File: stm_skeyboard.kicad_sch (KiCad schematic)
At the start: 0 parts

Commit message: adjust paths for kicanvas
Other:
- sheet main: file sheets/mcu.kicad_sch -> mcu.kicad_sch
- sheet matrix: file sheets/matrix.kicad_sch -> matrix.kicad_sch
- company: (none) -> https://github.com/Challmymind
- title: (none) -> Keyboard based on STM32L0xx
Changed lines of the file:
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@@
 	(generator_version "8.0")
 	(paper "A4")
+	(title_block
+		(title "Keyboard based on STM32L0xx")
+		(date "2024-04-28")
+		(rev "0.1")
+		(company "https://github.com/Challmymind")
+	)
 	(wire
 		(pts
@@
 			)
 		)
-		(property "Sheetfile" "sheets/matrix.kicad_sch"
+		(property "Sheetfile" "matrix.kicad_sch"
 			(at 184.15 104.7246 0)
 			(effects
@@
 			)
 		)
-		(property "Sheetfile" "sheets/mcu.kicad_sch"
+		(property "Sheetfile" "mcu.kicad_sch"
 			(at 91.44 80.5946 0)
 			(effects

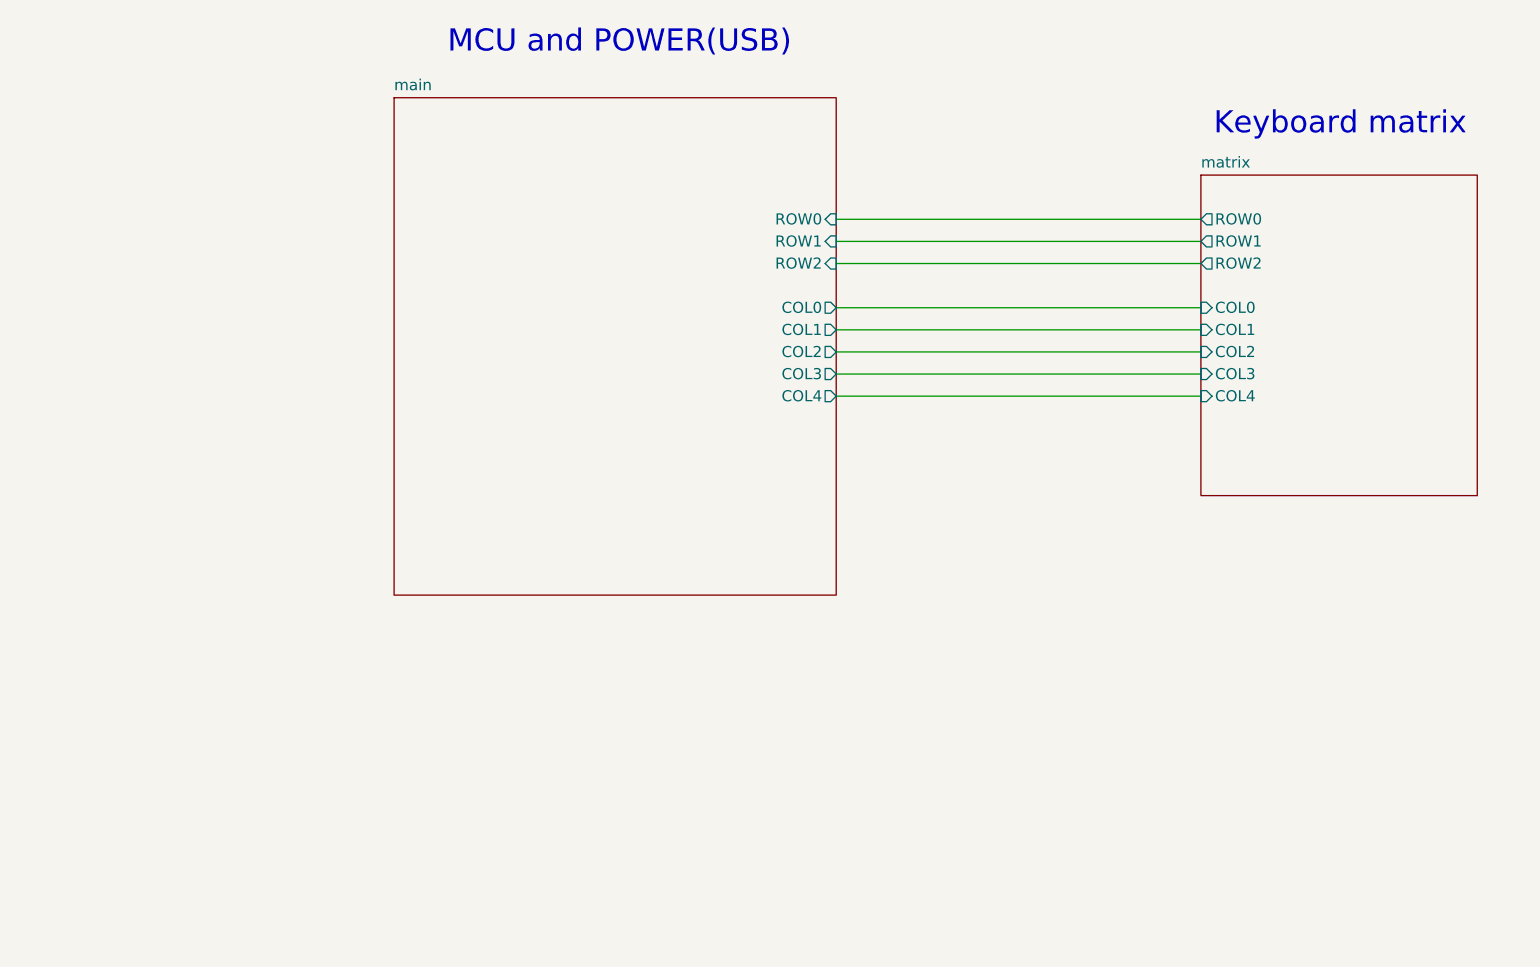
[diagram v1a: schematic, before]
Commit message: moved usb to another sheet, cleared ERC violations
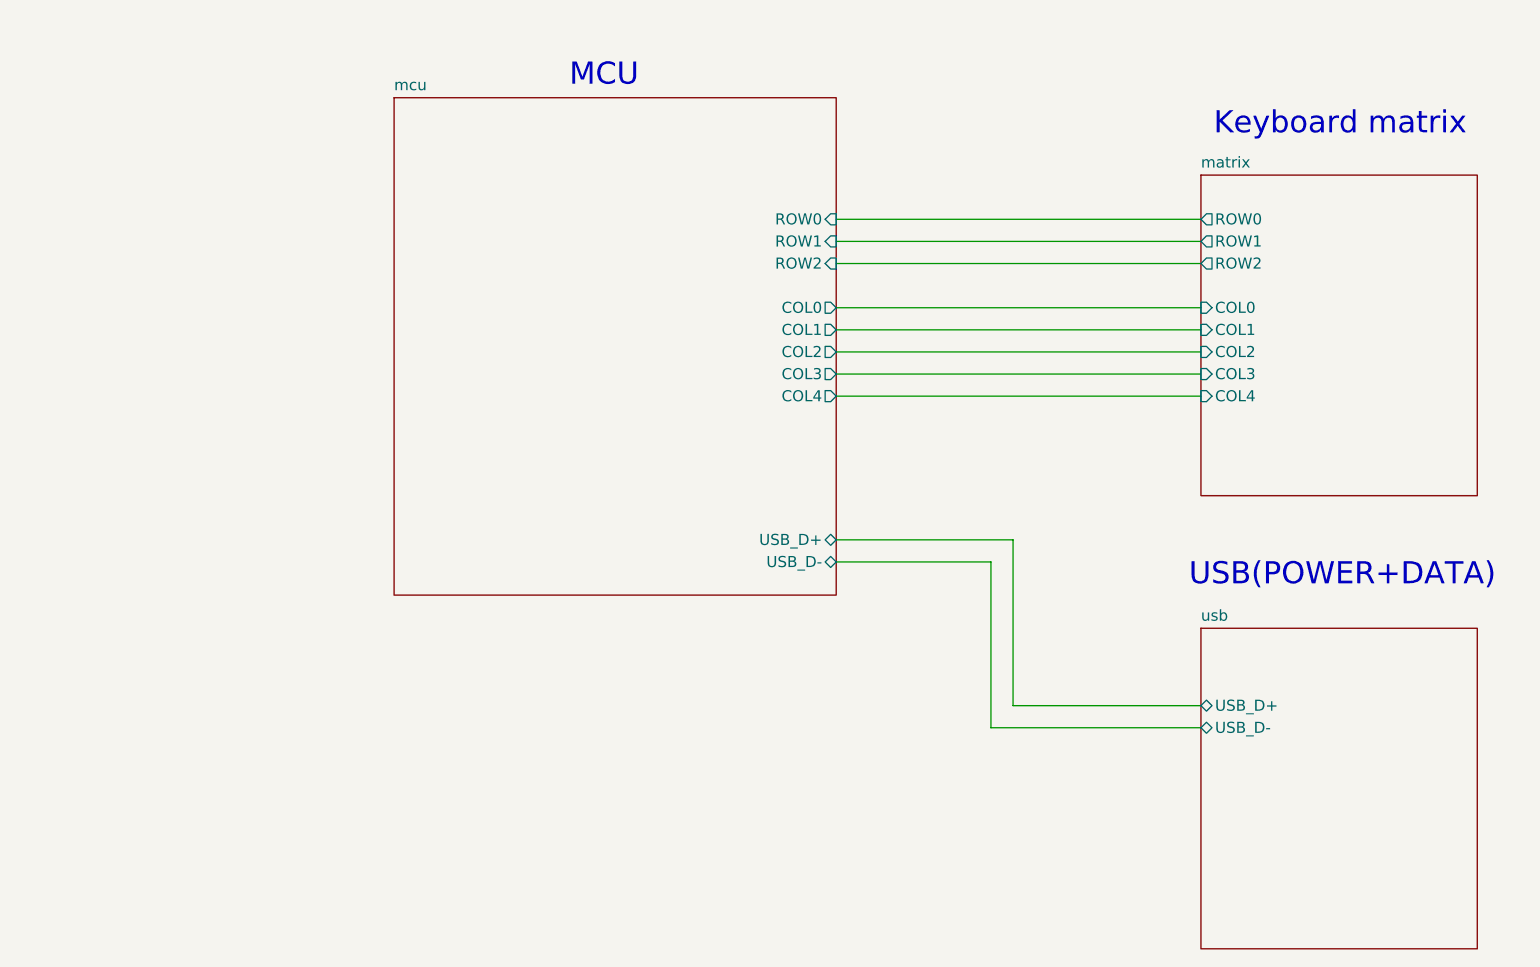
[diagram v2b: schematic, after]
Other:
- sheet main renamed mcu
- added sheet usb (usb.kicad_sch)
- sheet mcu ports: added USB_D+, USB_D-; removed none
- note added: "MCU"
- note added: "USB(POWER+DATA)"
- note removed: "MCU and POWER(USB)"
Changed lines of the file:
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@@
+	(wire
+		(pts
+			(xy 160.02 111.76) (xy 160.02 130.81)
+		)
+		(stroke
+			(width 0)
+			(type default)
+		)
+	)
 	(wire
 		(pts
@@
 	(wire
 		(pts
+			(xy 162.56 109.22) (xy 162.56 128.27)
+		)
+		(stroke
+			(width 0)
+			(type default)
+		)
+	)
+	(wire
+		(pts
+			(xy 142.24 109.22) (xy 162.56 109.22)
+		)
+		(stroke
+			(width 0)
+			(type default)
+		)
+	)
+	(wire
+		(pts
+			(xy 160.02 130.81) (xy 184.15 130.81)
+		)
+		(stroke
+			(width 0)
+			(type default)
+		)
+	)
+	(wire
+		(pts
 			(xy 142.24 87.63) (xy 184.15 87.63)
 		)
@@
 	(wire
 		(pts
+			(xy 142.24 111.76) (xy 160.02 111.76)
+		)
+		(stroke
+			(width 0)
+			(type default)
+		)
+	)
+	(wire
+		(pts
 			(xy 142.24 90.17) (xy 184.15 90.17)
 		)
@@
 	(wire
 		(pts
+			(xy 162.56 128.27) (xy 184.15 128.27)
+		)
+		(stroke
+			(width 0)
+			(type default)
+		)
+	)
+	(wire
+		(pts
 			(xy 142.24 82.55) (xy 184.15 82.55)
 		)
@@
 		)
 	)
-	(text "MCU and POWER(USB)\n"
+	(text "MCU"
 		(exclude_from_sim no)
-		(at 117.348 52.07 0)
+		(at 115.57 55.88 0)
 		(effects
 			(font
@@
 		)
 	)
+	(text "USB(POWER+DATA)"
+		(exclude_from_sim no)
+		(at 200.406 113.284 0)
+		(effects
+			(font
+				(size 2.54 2.54)
+			)
+		)
+	)
 	(sheet
 		(at 184.15 67.31)
@@
 	)
 	(sheet
+		(at 184.15 119.38)
+		(size 31.75 36.83)
+		(fields_autoplaced yes)
+		(stroke
+			(width 0.1524)
+			(type solid)
+		)
+		(fill
+			(color 255 255 194 1.0000)
+		)
+		(property "Sheetname" "usb"
+			(at 184.15 118.6684 0)
+			(effects
+				(font
+					(size 1.27 1.27)
+				)
+				(justify left bottom)
+			)
+		)
+		(property "Sheetfile" "usb.kicad_sch"
+			(at 184.15 156.7946 0)
+			(effects
+				(font
+					(size 1.27 1.27)
+				)
+				(justify left top)
+				(hide yes)
+			)
+		)
+		(pin "USB_D+" bidirectional
+			(at 184.15 128.27 180)
+			(effects
+				(font
+					(size 1.27 1.27)
+				)
+				(justify left)
+			)
+		)
+		(pin "USB_D-" bidirectional
+			(at 184.15 130.81 180)
+			(effects
+				(font
+					(size 1.27 1.27)
+				)
+				(justify left)
+			)
+		)
+		(instances
+			(project "stm_skeyboard"
+				(path "/f8cbad95-1fac-4ee0-b4c1-fc27b4678331"
+					(page "4")
+				)
+			)
+		)
+	)
+	(sheet
 		(at 91.44 58.42)
 		(size 50.8 57.15)
@@
 			(color 255 255 194 1.0000)
 		)
-		(property "Sheetname" "main"
+		(property "Sheetname" "mcu"
 			(at 91.44 57.7084 0)
 			(effects
@@
 			(effects
 				(font
+					(size 1.27 1.27)
+				)
+				(justify right)
+			)
+		)
+		(pin "USB_D+" bidirectional
+			(at 142.24 109.22 0)
+			(effects
+				(font
+					(size 1.27 1.27)
+				)
+				(justify right)
+			)
+		)
+		(pin "USB_D-" bidirectional
+			(at 142.24 111.76 0)
+			(effects
+				(font

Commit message: completed 0.1 schematic design
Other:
- note added: "Make this connection as short as possible"
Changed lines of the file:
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@@
+		)
+	)
+	(text "Make this connection as short as possible\n"
+		(exclude_from_sim no)
+		(at 165.608 107.442 0)
+		(effects
+			(font
+				(size 1.27 1.27)
+			)
 		)
 	)
@@
 		)
 		(property "Sheetfile" "mcu.kicad_sch"
-			(at 91.44 80.5946 0)
-			(effects
-				(font
+			(at 91.186 116.84 0)
+			(effects
+				(font

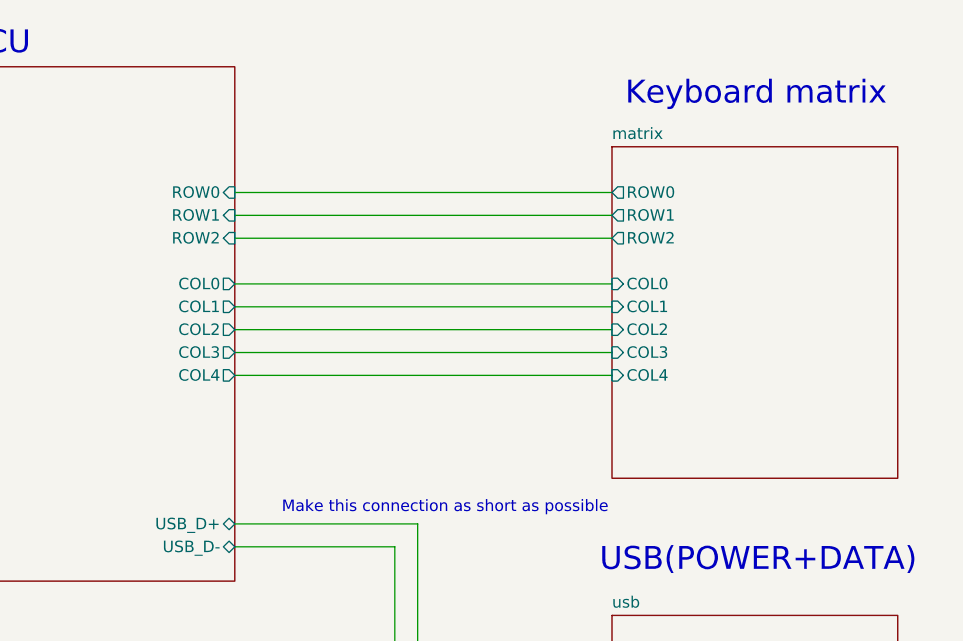
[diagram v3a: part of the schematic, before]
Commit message: switched to bigger matrix, adjusted mcu pins, started pcb layout
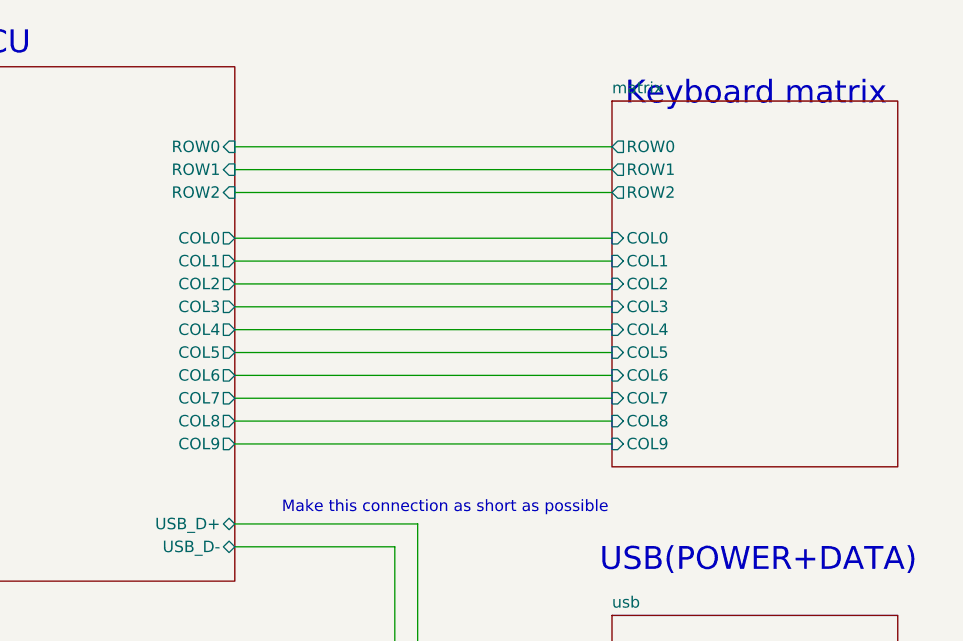
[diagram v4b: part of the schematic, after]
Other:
- sheet matrix ports: added COL5, COL6, COL7, COL8, COL9; removed none
- sheet mcu ports: added COL5, COL6, COL7, COL8, COL9; removed none

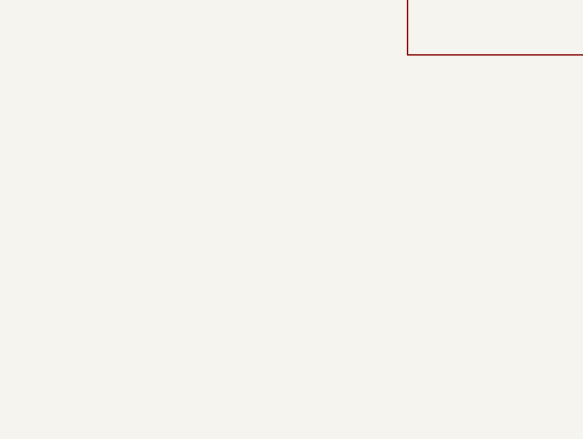
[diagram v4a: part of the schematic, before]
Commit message: added 3d models, completed 0.1
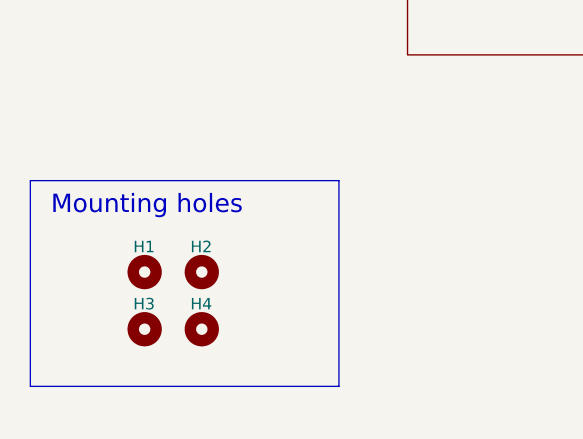
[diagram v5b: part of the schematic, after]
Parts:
- added H1, H2, H3, H4: MountingHole, MountingHole:MountingHole_2.1mm, symbol Mechanical:MountingHole
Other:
- note added: "Mounting holes"
